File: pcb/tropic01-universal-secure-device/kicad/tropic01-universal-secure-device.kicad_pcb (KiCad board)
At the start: 4 copper layers, 42.7 x 36 mm, 94 parts, among them J1 USB4105-GF-A, J2 ER-TFT024IPS-3 50P FFC, J6 SM04B-SRSS-TB, J7 SWD_TC2030, J9 S2B-PH-SM4-TB, SW1 EVQP7J01P, U1 STM32U585VIT6, U10 BQ24074RGTR, U11 OPTIGA-TRUST-M-SLS32AIA, U13 TPS22917DBVR, U14 TPS22917DBVR, U15 TPS61165DBVR, U2 TR01-C2P-T301, U3 TPS62840DLCR, U4 TPS22917DBVR, U5 W25Q128JVSIQ, U7 TPD4E05U06DQAR, U8 TPS2553DBVR, U9 ST25R3916B-AQET, X1 16MHz, X3 FA-238 27.12MHz

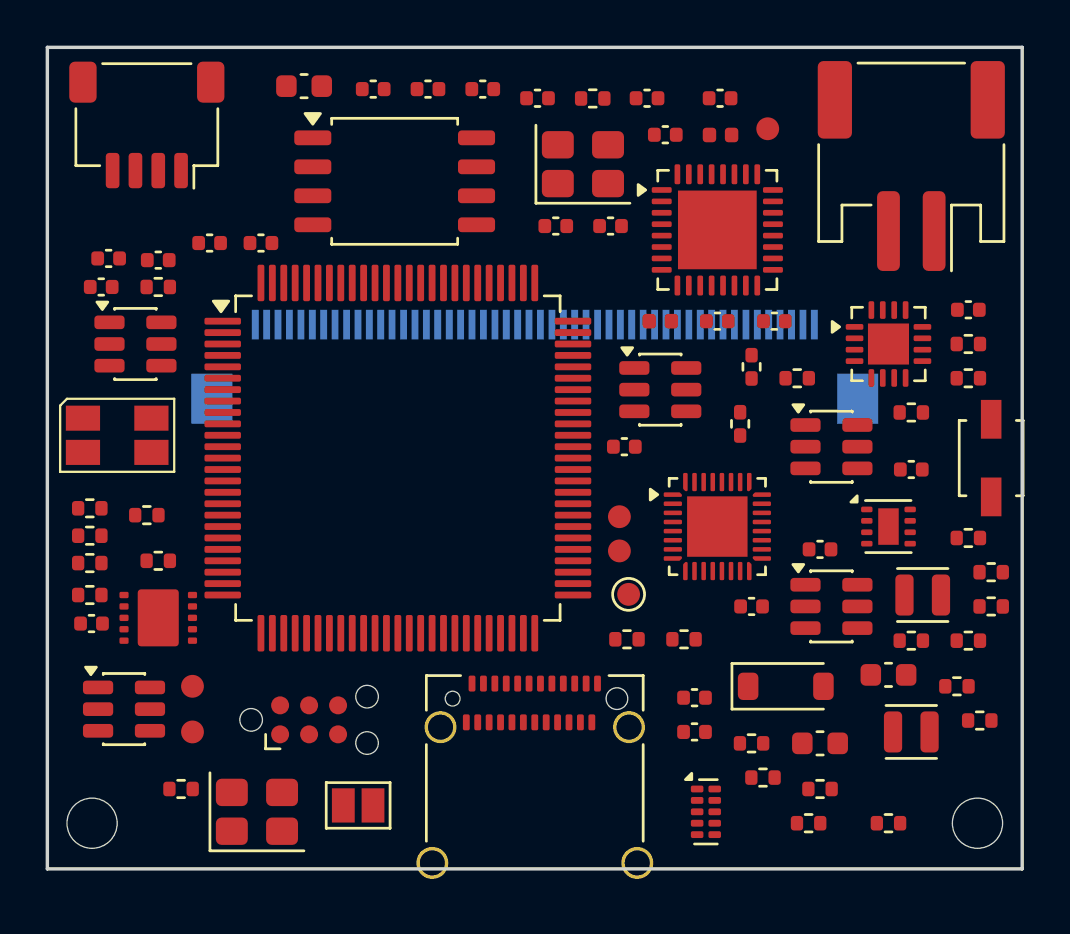
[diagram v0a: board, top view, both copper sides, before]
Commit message: improve(pcb): place TROPIC01 adjacent to the STM32 secure-SPI pins
TROPIC01 (U2) was on the opposite side from the STM32's secure-SPI pins -> the
secure SPI channel was ~16mm. Move U2 directly below the STM32's SPI pins (oriented
so its SPI pins face up), relocating J7 (SWD) to the old TROPIC area. Secure SPI now
~2.4mm centroid-to-centroid (much shorter = better integrity + harder to tap).
Re-clustered passives; re-tightened STM32 (2.6mm) and OPTIGA (5.3mm) decoupling.
DRC clean (only the accepted USB-C edge posts); B.Cu still only J2.
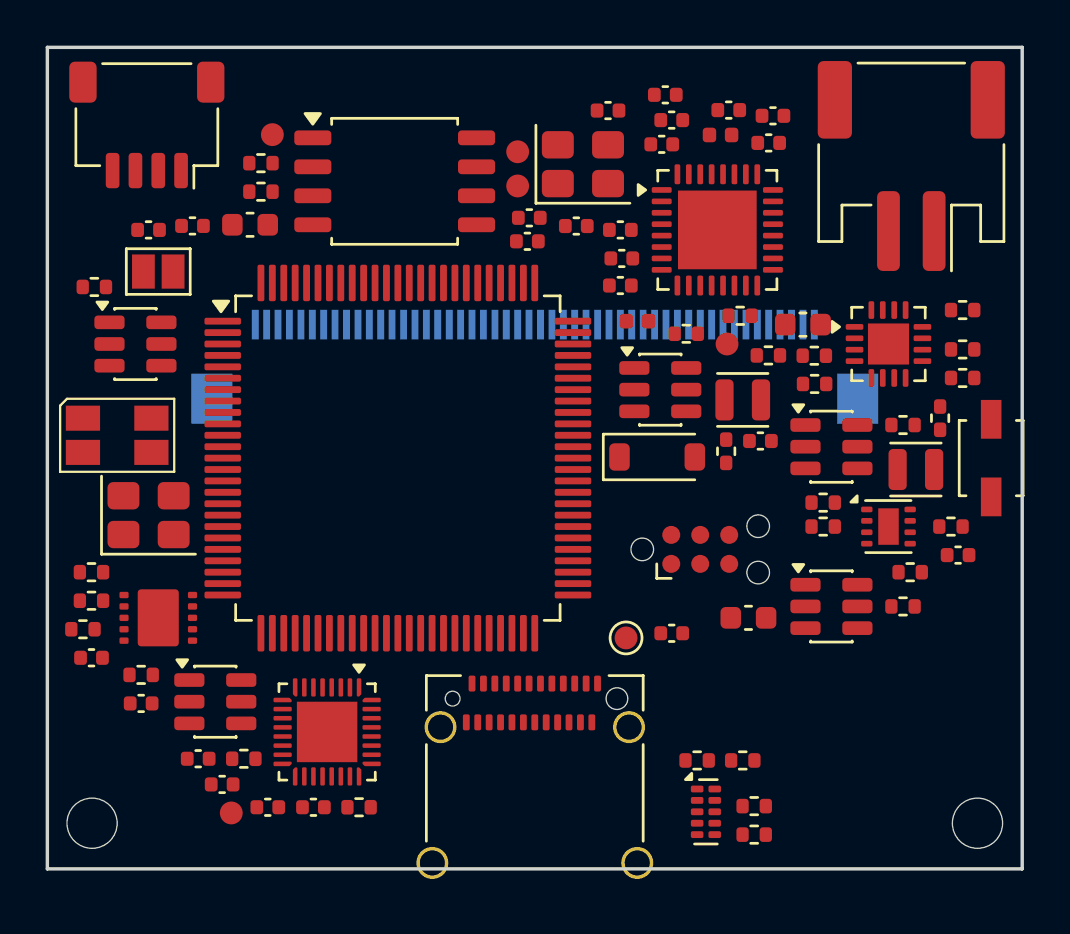
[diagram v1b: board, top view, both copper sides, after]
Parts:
- moved C7 29.2 mm to (38.0, 59.7)
- moved JP1 25.0 mm to (15.5, 43.8)
- moved TP_BOOT0 24.4 mm to (20.5, 37.8)
- moved C16 24.0 mm to (14.8, 62.8)
- moved C17 21.9 mm to (17.2, 65.2)
- moved C5 21.1 mm to (22.3, 67.3)
- moved C4 21.0 mm to (18.3, 66.3)
- moved C41 19.9 mm to (38.0, 37.2)
- moved U2 19.3 mm to (22.9, 64.0), turned to -90 degrees
- moved C3 19.0 mm to (20.3, 67.3)
- moved R11 18.8 mm to (41.0, 45.8)
- moved J7 18.7 mm to (39.2, 56.0)
- moved C15 18.4 mm to (43.8, 46.1)
- moved C40 17.6 mm to (42.4, 37.0)
- moved TP_UART_RX 16.6 mm to (31.2, 38.6)
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
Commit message: improve(pcb): CT caps adjacent to load switches + rebalance backlight to bottom-right
(a) Move the load-switch soft-start caps onto their switch CT pins: C6->U4 1.5mm,
C8->U13 1.5mm, C7->U14 3.2mm (were 22-51mm) - critical for switch timing.
(b) Relocate the backlight boost (U15+L15) into the previously-empty bottom-right
to relieve congestion. TROPIC secure-SPI preserved at 2.4mm; DRC clean (only the
accepted USB-C edge posts).
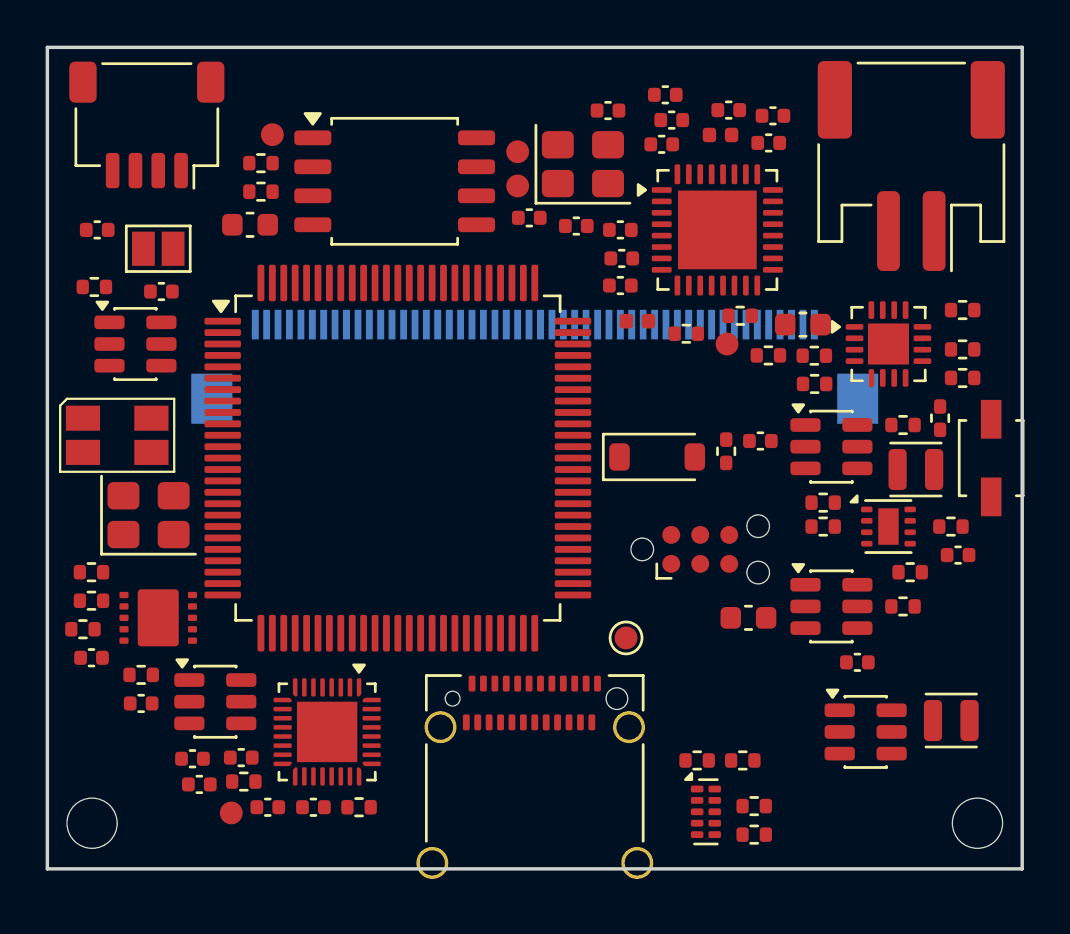
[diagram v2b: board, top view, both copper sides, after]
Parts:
- moved C7 26.9 mm to (15.6, 44.7)
- moved C8 23.4 mm to (46.1, 61.0)
- moved C6 23.4 mm to (19.1, 65.1)
- moved U15 17.5 mm to (46.5, 64.0)
- moved L15 16.8 mm to (50.2, 63.5)
- moved C19 2.25 mm to (12.8, 42.0)
- moved C4 1.00 mm to (17.3, 66.3)
- moved JP1 1.00 mm to (15.5, 42.8)
- moved R5 1.00 mm to (19.2, 66.2)
- moved C17 0.25 mm to (17.0, 65.2)
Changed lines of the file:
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@@
 	(footprint "Capacitor_SMD:C_0402_1005Metric"
 		(layer "F.Cu")
-		(at 17.25 65.175)
+		(at 17 65.175)
 		(descr "Capacitor SMD 0402 (1005 Metric), square (rectangular) end terminal, IPC-7351 nominal, (Body size source: IPC-SM-782 page 76, https://www.pcb-3d.com/wordpress/wp-content/uploads/ipc-sm-782a_amendment_1_and_2.pdf)")
 		(tags "capacitor")
@@
 	(footprint "SolderJumper-2_P1.3mm_Open_Pad1.0x1.5mm"
 		(layer "F.Cu")
-		(at 15.5 43.825)
+		(at 15.5 42.825)
 		(descr "SMD Solder Jumper, 1x1.5mm Pads, 0.3mm gap, open")
 		(tags "solder jumper open")
@@
 	(footprint "Inductor_SMD:L_Wuerth_PMFI-201610_PMCI-compatible"
 		(layer "F.Cu")
-		(at 41.1125 49.45)
+		(at 50.25 63.5)
 		(descr "Inductor, Wuerth, PMFI-201610_PMCI-compatible, 2.0x1.6x1.0mm, (https://www.we-online.com/components/products/datasheet/74479320165110.pdf)")
 		(tags "Würth SMT")
@@
 	(footprint "Capacitor_SMD:C_0402_1005Metric"
 		(layer "F.Cu")
-		(at 38 59.675)
+		(at 15.6375 44.7)
 		(descr "Capacitor SMD 0402 (1005 Metric), square (rectangular) end terminal, IPC-7351 nominal, (Body size source: IPC-SM-782 page 76, https://www.pcb-3d.com/wordpress/wp-content/uploads/ipc-sm-782a_amendment_1_and_2.pdf)")
 		(tags "capacitor")
@@
 	(footprint "Package_TO_SOT_SMD:SOT-23-6"
 		(layer "F.Cu")
-		(at 37.5 49)
+		(at 46.5 64)
 		(descr "SOT, 6 Pin (JEDEC MO-178 Var AB https://www.jedec.org/document_search?search_api_views_fulltext=MO-178)")
 		(tags "SOT TO_SOT_SMD")
@@
 	(footprint "Capacitor_SMD:C_0402_1005Metric"
 		(layer "F.Cu")
-		(at 17 41.825)
+		(at 19.1375 65.125)
 		(descr "Capacitor SMD 0402 (1005 Metric), square (rectangular) end terminal, IPC-7351 nominal, (Body size source: IPC-SM-782 page 76, https://www.pcb-3d.com/wordpress/wp-content/uploads/ipc-sm-782a_amendment_1_and_2.pdf)")
 		(tags "capacitor")
@@
 	(footprint "Resistor_SMD:R_0402_1005Metric"
 		(layer "F.Cu")
-		(at 19.25 65.175)
+		(at 19.25 66.175)
 		(descr "Resistor SMD 0402 (1005 Metric), square (rectangular) end terminal, IPC-7351 nominal, (Body size source: IPC-SM-782 page 72, https://www.pcb-3d.com/wordpress/wp-content/uploads/ipc-sm-782a_amendment_1_and_2.pdf)")
 		(tags "resistor")
@@
 	(footprint "Capacitor_SMD:C_0402_1005Metric"
 		(layer "F.Cu")
-		(at 31.674999 42.5)
+		(at 46.1375 60.95)
 		(descr "Capacitor SMD 0402 (1005 Metric), square (rectangular) end terminal, IPC-7351 nominal, (Body size source: IPC-SM-782 page 76, https://www.pcb-3d.com/wordpress/wp-content/uploads/ipc-sm-782a_amendment_1_and_2.pdf)")
 		(tags "capacitor")
@@
 	(footprint "Capacitor_SMD:C_0402_1005Metric"
 		(layer "F.Cu")
-		(at 15.075 42)
+		(at 12.825 42)
 		(descr "Capacitor SMD 0402 (1005 Metric), square (rectangular) end terminal, IPC-7351 nominal, (Body size source: IPC-SM-782 page 76, https://www.pcb-3d.com/wordpress/wp-content/uploads/ipc-sm-782a_amendment_1_and_2.pdf)")
 		(tags "capacitor")
@@
 	(footprint "Capacitor_SMD:C_0402_1005Metric"
 		(layer "F.Cu")
-		(at 18.3 66.3)
+		(at 17.3 66.3)
 		(descr "Capacitor SMD 0402 (1005 Metric), square (rectangular) end terminal, IPC-7351 nominal, (Body size source: IPC-SM-782 page 76, https://www.pcb-3d.com/wordpress/wp-content/uploads/ipc-sm-782a_amendment_1_and_2.pdf)")
 		(tags "capacitor")

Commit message: improve(pcb) iter1: NFC closer to STM32 + 4 corner holes + connectors inward
Move U9(NFC) toward the STM32 NFC-SPI pins -> NFC SPI 14.5->8.7mm (the #1 unrouted
cluster). Move J6/J9 inward off the top corners (original Y) and add MH3/MH4 ->
4 corner mounting holes. Re-cluster passives (crystals/flash re-anchored). TROPIC
secure-SPI kept 2.4mm. DRC clean (only USB-C edge); B.Cu only J2.
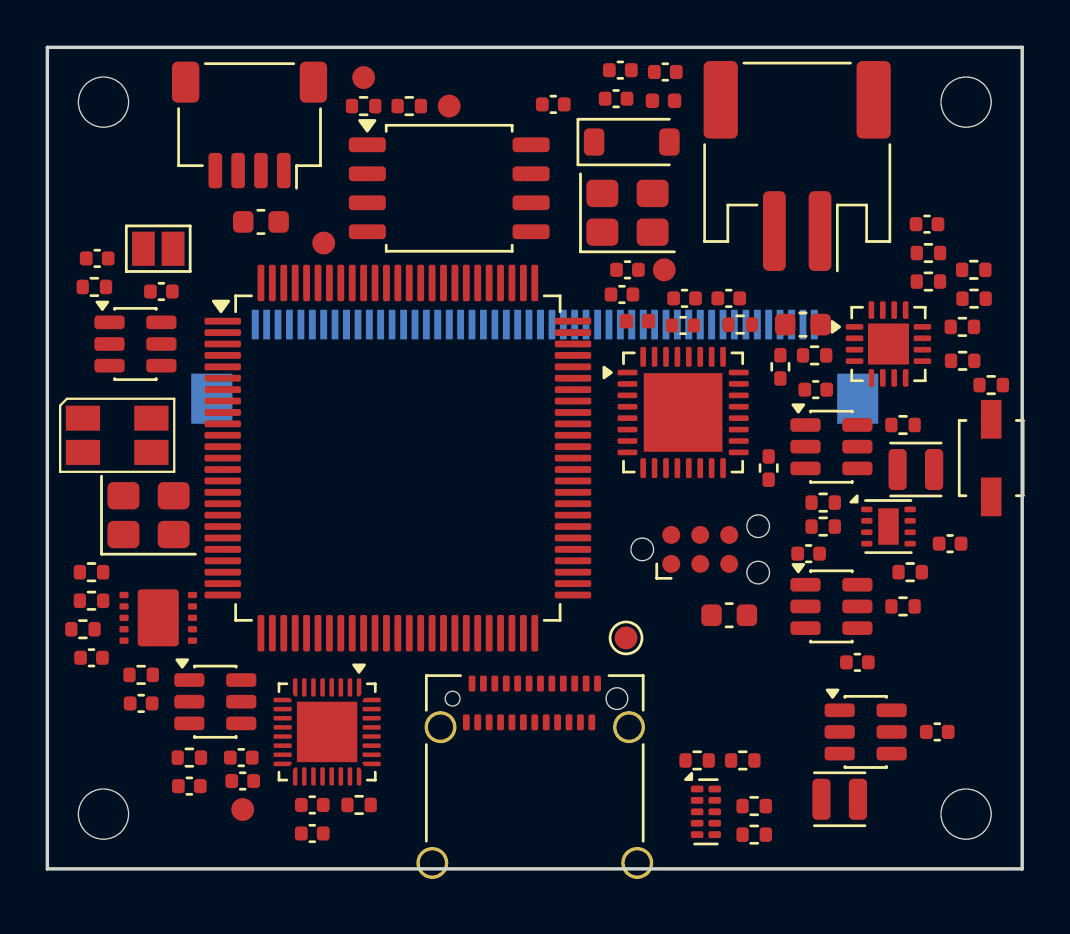
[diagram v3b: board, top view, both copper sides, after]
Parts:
- added MH3: M2_CASE_SCREW_CLEARANCE, nSealr_Mechanical:MountingHole_M2_Clearance_NPTH, F.Cu at (13.1, 36.4)
- added MH4: M2_CASE_SCREW_CLEARANCE, nSealr_Mechanical:MountingHole_M2_Clearance_NPTH, F.Cu at (50.9, 36.4)
- moved C39 18.1 mm to (44.0, 56.2)
- moved C13 14.9 mm to (49.6, 64.0)
- moved D15 13.8 mm to (36.2, 38.1)
- moved C36 12.7 mm to (44.3, 49.0)
- moved R17 11.3 mm to (51.2, 43.8)
- moved R11 10.3 mm to (51.2, 45.0)
- moved TP_UART_TX 8.86 mm to (22.8, 42.6)
- moved R9 8.59 mm to (50.7, 46.2)
- moved C40 8.25 mm to (49.2, 41.8)
- moved U9 8.14 mm to (38.5, 50.0)
- moved R20 7.35 mm to (42.8, 48.0)
- moved C35 7.03 mm to (36.1, 43.8)
- moved R7 6.96 mm to (26.5, 36.6)
- moved C34 6.46 mm to (35.6, 36.2)
- moved L15 5.98 mm to (45.4, 67.0)
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
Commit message: feat(pcb): rounded corners R=2.5mm (corner holes seated in fillets)
Replace the rectangular Edge.Cuts with 4 segments + 4 R=2.5mm arcs.
Each M2 corner hole (MH1-4) sits at its fillet centre (~1.3mm edge
clearance). Connectors already inboard, so no part is clipped. DRC
unchanged: only the accepted USB-C edge posts + pre-existing cosmetic
silk (SW1 side-button outline, U10/C15).
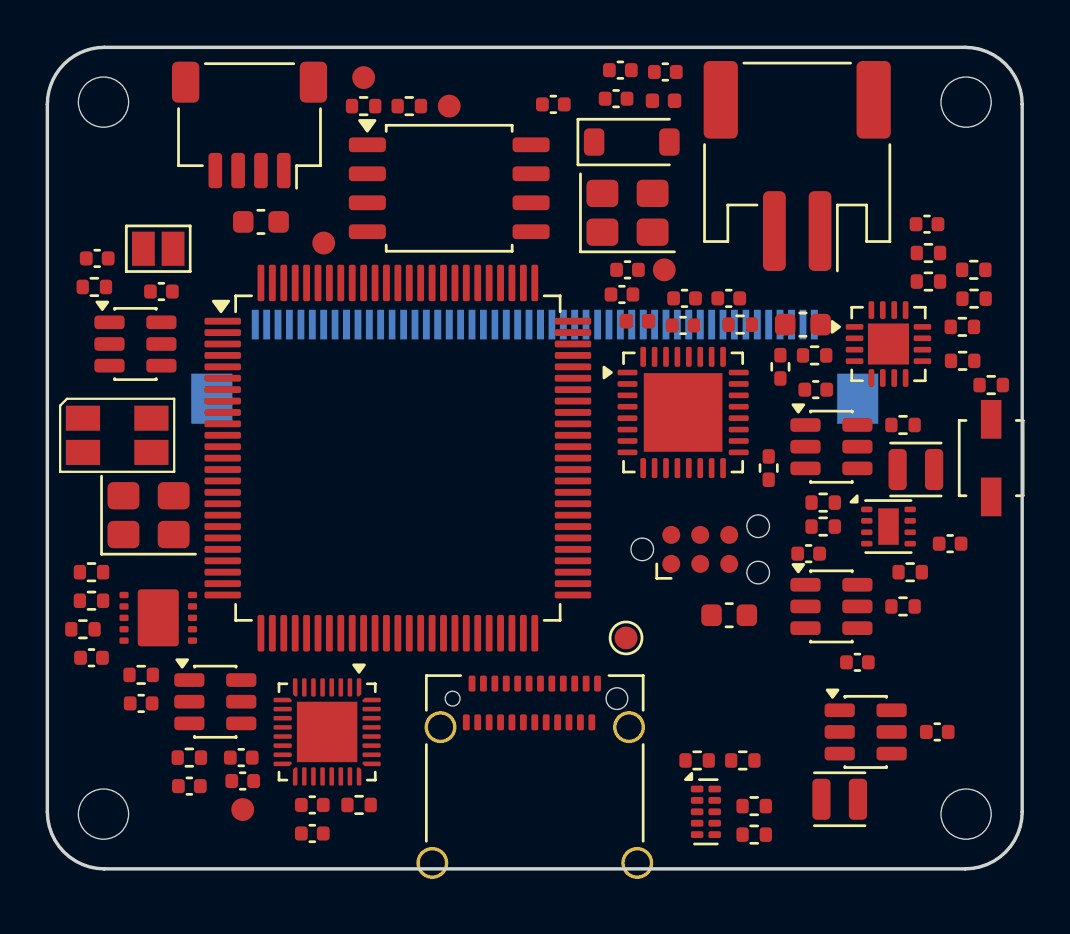
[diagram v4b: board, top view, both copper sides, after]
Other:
- outline, holes or cut-outs redrawn
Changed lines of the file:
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@@
 		(embedded_fonts no)
 	)
-	(gr_rect
-		(start 10.64 34)
-		(end 53.36 70)
+	(gr_arc
+		(start 10.64 36.5)
+		(mid 11.372233 34.732233)
+		(end 13.14 34)
 		(stroke
 			(width 0.15)
-			(type solid)
+			(type default)
 		)
-		(fill no)
-		(locked yes)
 		(layer "Edge.Cuts")
 	)
+	(gr_line
+		(start 10.64 67.5)
+		(end 10.64 36.5)
+		(stroke
+			(width 0.15)
+			(type default)
+		)
+		(layer "Edge.Cuts")
+	)
+	(gr_line
+		(start 13.14 34)
+		(end 50.86 34)
+		(stroke
+			(width 0.15)
+			(type default)
+		)
+		(layer "Edge.Cuts")
+	)
+	(gr_arc
+		(start 13.14 70)
+		(mid 11.372233 69.267766)
+		(end 10.64 67.5)
+		(stroke
+			(width 0.15)
+			(type default)
+		)
+		(layer "Edge.Cuts")
+	)
+	(gr_arc
+		(start 50.86 34)
+		(mid 52.627766 34.732233)
+		(end 53.36 36.5)
+		(stroke
+			(width 0.15)
+			(type default)
+		)
+		(layer "Edge.Cuts")
+	)
+	(gr_line
+		(start 50.86 70)
+		(end 13.14 70)
+		(stroke
+			(width 0.15)
+			(type default)
+		)
+		(layer "Edge.Cuts")
+	)
+	(gr_line
+		(start 53.36 36.5)
+		(end 53.36 67.5)
+		(stroke
+			(width 0.15)
+			(type default)
+		)
+		(layer "Edge.Cuts")
+	)
+	(gr_arc
+		(start 53.36 67.5)
+		(mid 52.627766 69.267766)
+		(end 50.86 70)
+		(stroke
+			(width 0.15)
+			(type default)
+		)
+		(layer "Edge.Cuts")
+	)

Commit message: feat(pcb): from-scratch placement rebuild (all 90 parts, DRC-clean)
Rebuilt the placement from an empty board, top-down:
- STM32 orient 0 (only orientation that keeps LED on the left edge and
  NFC SPI toward the top antenna; keeps TROPIC SPI short).
- Abstract zones: secure(TROPIC)+flash bottom-left (S-side pins),
  OPTIGA top-left (N-side), NFC right-center toward antenna, power as a
  right-side flow spine (USB-C->U8->U10->U3), LED/HSE left, connectors
  inboard top, USB-C bottom-center.
- Flash moved adjacent to QSPI pins (fixes the old top placement).
- J7 SWD reserved in the skeleton so it fits.
- Passives clustered to their ICs and aligned to a 0.5/1.0mm grid
  (size-first packing so bulk caps fit). DISP1+J2 only on B.Cu.
DRC clean except the accepted USB-C edge posts + SW1 side-button silk.
0 tracks/zones (clean base for routing).
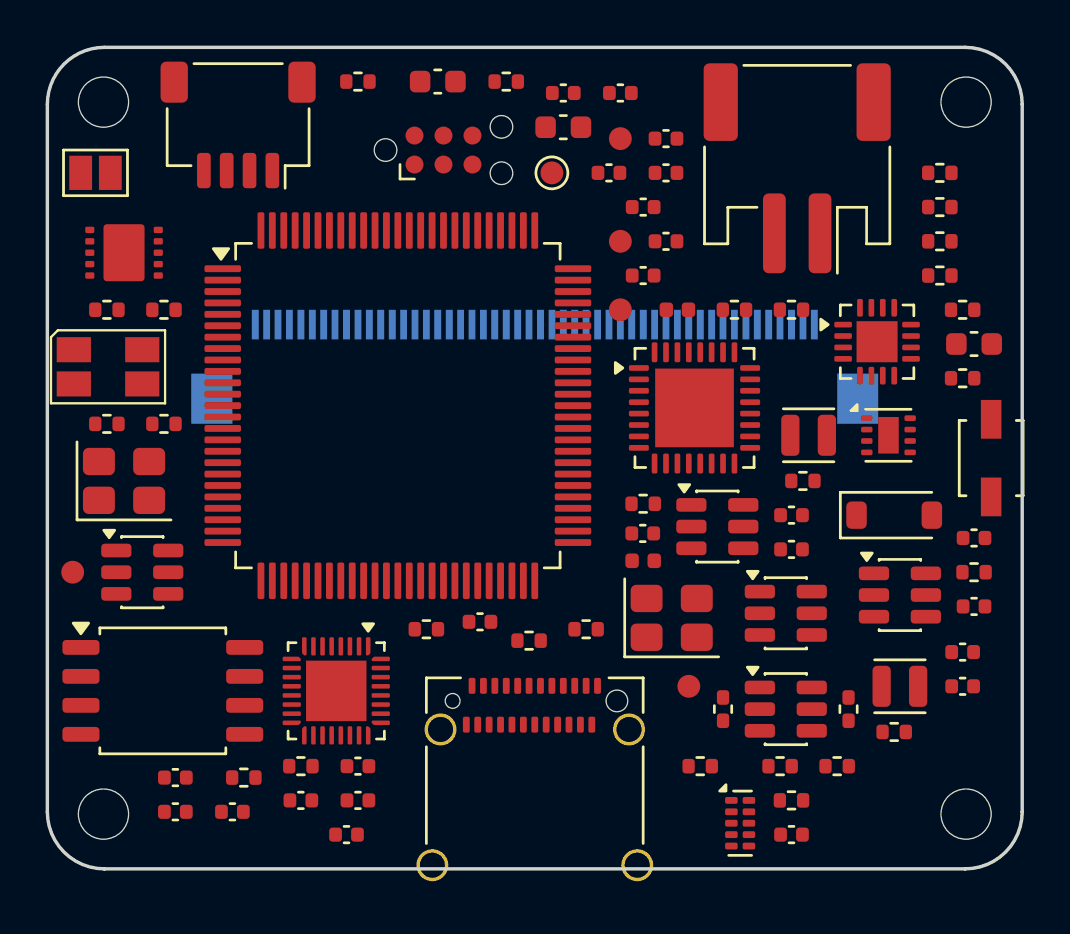
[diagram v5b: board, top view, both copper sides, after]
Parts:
- moved C7 38.5 mm to (50.8, 60.5)
- moved U14 30.8 mm to (43.0, 58.8)
- moved C1 26.6 mm to (27.8, 35.5)
- moved U5 25.3 mm to (15.7, 62.2)
- moved C32 24.8 mm to (43.2, 68.5)
- moved C19 23.1 mm to (29.6, 59.2)
- moved J7 20.8 mm to (28.0, 38.5)
- moved TP_UART_GND 20.6 mm to (32.8, 39.5)
- moved L31 20.2 mm to (36.8, 56.5)
- moved D15 20.0 mm to (47.8, 54.5)
- moved C34 19.1 mm to (36.7, 55.3)
- moved TP_3V3 18.3 mm to (38.8, 62.0)
- moved X3 17.9 mm to (38.0, 59.0)
- moved C39 17.8 mm to (37.8, 39.5)
- moved R6 16.1 mm to (13.2, 45.5)
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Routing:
- removed copper zone on In1.Cu, net GND
